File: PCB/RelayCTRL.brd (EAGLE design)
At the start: 46.7 x 22.3 mm, 20 parts, among them Q2 BC848 30V 100mA, Q3 IRLML6402, U1 SN74HC4066D

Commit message: fixed pcb error
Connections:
- removed net N$1: B1.9, R2.2
- net 5V: now also R2.2
- net IR: now also B1.9
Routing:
- net N$1: track 13.3 -> 0.00 mm
- net IR: track 6.76 -> 19.3 mm
- net 5V: track 81.3 -> 92.9 mm
- net S1: track 22.2 -> 19.7 mm
- net BT2: track 39.7 -> 38.1 mm

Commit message: PCB Update
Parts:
- added Q1: BC848 30V 100mA, SparkFun-DiscreteSemi:SOT23-3
- added R7: 1k, rcl:R0603
- renumbered 5V to BZ+, BZ to IR-, G to BZ-
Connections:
- new net BZ-: BZ-.TP, Q1.3
- new net N$1: B1.9, R2.2
- new net N$5: Q1.1, R7.2
- net 5V: no longer R2.2
- net GND: now also IR-.TP, Q1.2, U1.11, U1.8; no longer BZ-.TP
- net IR: no longer B1.9
- net S1: now also R7.1; no longer IR-.TP
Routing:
- net BZ-: track 0.00 -> 37.3 mm, vias 0 -> 1
- net S1: track 19.7 -> 4.01 mm
- net N$1: track 0.00 -> 13.3 mm
- net IR: track 19.3 -> 6.76 mm
- net 5V: track 92.9 -> 81.3 mm
- net N$5: track 0.00 -> 10.3 mm
- net BT2: track 38.1 -> 39.4 mm
- net BT4: track 16.1 -> 17.2 mm
- net SCL: track 24.9 -> 24.7 mm, vias 1 -> 0

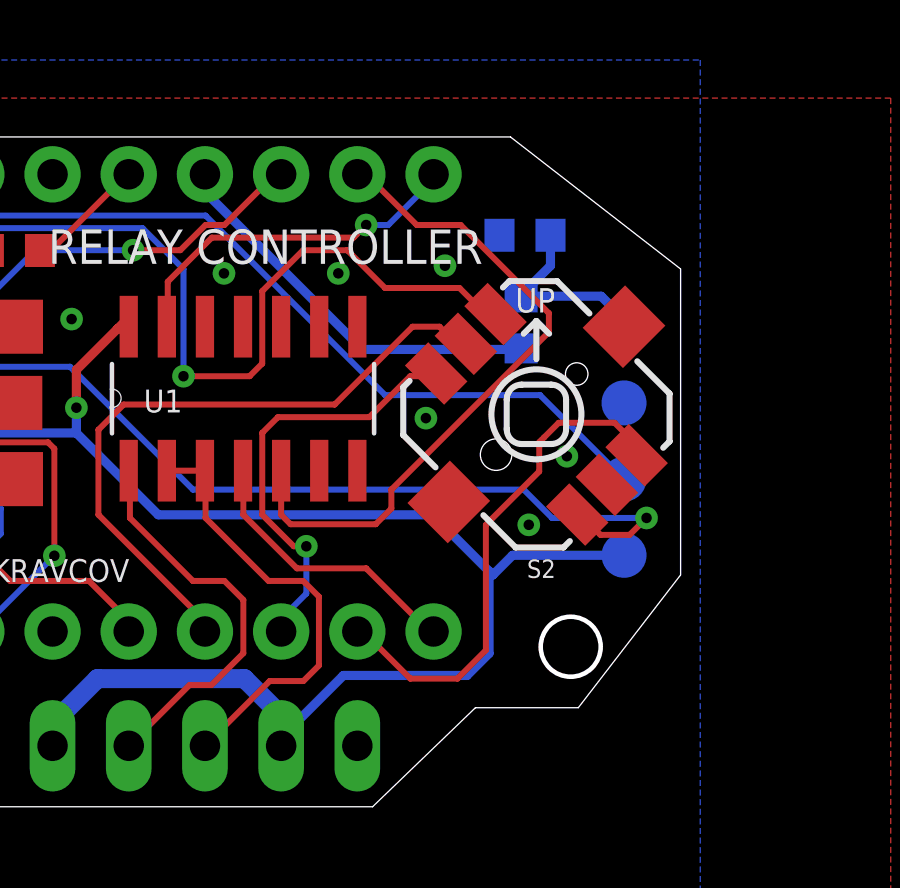
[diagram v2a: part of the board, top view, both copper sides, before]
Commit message: Corrected PCB bug (IR diode)
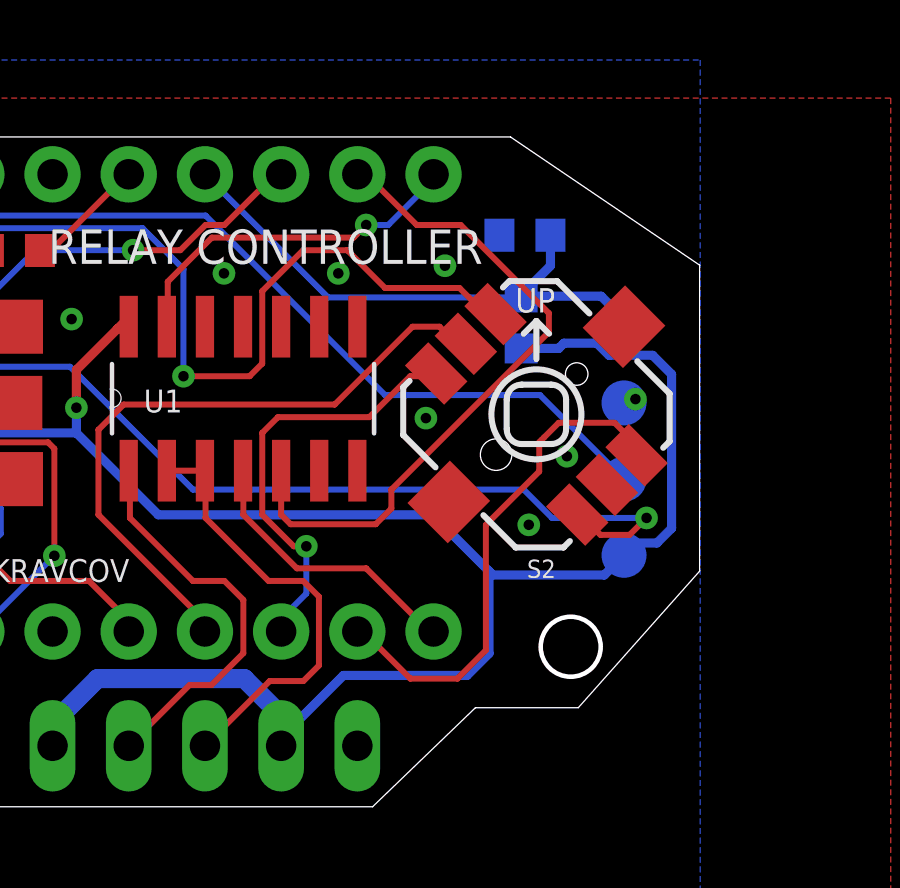
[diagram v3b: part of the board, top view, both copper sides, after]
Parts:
- moved IR+ 2.79 mm to (38.1, 100.3)
- moved IR- 2.79 mm to (38.1, 103.1)
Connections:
- removed net N$1: B1.9, R2.2
- net 5V: now also R2.2
- net GND: now also IR+.TP; no longer IR-.TP
- net IR: now also B1.9, IR-.TP; no longer IR+.TP
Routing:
- net N$1: track 13.3 -> 0.00 mm
- net 5V: track 81.3 -> 93.9 mm
- net IR: track 6.76 -> 19.0 mm
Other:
- board size 46.7 x 22.3 mm -> 47.4 x 22.3 mm
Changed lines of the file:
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@@
 <drawing>
 <settings>
-<setting alwaysvectorfont="no"/>
+<setting alwaysvectorfont="yes"/>
 <setting verticaltext="up"/>
 </settings>
 <grid distance="50" unitdist="mil" unit="mil" style="lines" multiple="1" display="no" altdistance="5" altunitdist="mil" altunit="mil"/>
 <layers>
-<layer number="1" name="Top" color="4" fill="1" visible="yes" active="yes"/>
+<layer number="1" name="Top" color="4" fill="1" visible="no" active="yes"/>
 <layer number="2" name="Route2" color="16" fill="1" visible="no" active="no"/>
 <layer number="3" name="Route3" color="17" fill="1" visible="no" active="no"/>
@@
 <layer number="14" name="Route14" color="22" fill="1" visible="no" active="no"/>
 <layer number="15" name="Route15" color="23" fill="1" visible="no" active="no"/>
-<layer number="16" name="Bottom" color="1" fill="1" visible="no" active="yes"/>
+<layer number="16" name="Bottom" color="1" fill="1" visible="yes" active="yes"/>
 <layer number="17" name="Pads" color="2" fill="1" visible="yes" active="yes"/>
 <layer number="18" name="Vias" color="2" fill="1" visible="yes" active="yes"/>
 <layer number="19" name="Unrouted" color="6" fill="1" visible="yes" active="yes"/>
 <layer number="20" name="Dimension" color="24" fill="1" visible="yes" active="yes"/>
-<layer number="21" name="tPlace" color="7" fill="1" visible="yes" active="yes"/>
-<layer number="22" name="bPlace" color="7" fill="1" visible="no" active="yes"/>
-<layer number="23" name="tOrigins" color="15" fill="1" visible="yes" active="yes"/>
-<layer number="24" name="bOrigins" color="15" fill="1" visible="no" active="yes"/>
-<layer number="25" name="tNames" color="7" fill="1" visible="yes" active="yes"/>
-<layer number="26" name="bNames" color="7" fill="1" visible="no" active="yes"/>
+<layer number="21" name="tPlace" color="7" fill="1" visible="no" active="yes"/>
+<layer number="22" name="bPlace" color="7" fill="1" visible="yes" active="yes"/>
+<layer number="23" name="tOrigins" color="15" fill="1" visible="no" active="yes"/>
+<layer number="24" name="bOrigins" color="15" fill="1" visible="yes" active="yes"/>
+<layer number="25" name="tNames" color="7" fill="1" visible="no" active="yes"/>
+<layer number="26" name="bNames" color="7" fill="1" visible="yes" active="yes"/>
 <layer number="27" name="tValues" color="7" fill="1" visible="no" active="yes"/>
 <layer number="28" name="bValues" color="7" fill="1" visible="no" active="yes"/>
@@
 <layer number="37" name="tTest" color="7" fill="1" visible="no" active="yes"/>
 <layer number="38" name="bTest" color="7" fill="1" visible="no" active="yes"/>
-<layer number="39" name="tKeepout" color="4" fill="11" visible="yes" active="yes"/>
-<layer number="40" name="bKeepout" color="1" fill="11" visible="no" active="yes"/>
-<layer number="41" name="tRestrict" color="4" fill="10" visible="yes" active="yes"/>
-<layer number="42" name="bRestrict" color="1" fill="10" visible="no" active="yes"/>
+<layer number="39" name="tKeepout" color="4" fill="11" visible="no" active="yes"/>
+<layer number="40" name="bKeepout" color="1" fill="11" visible="yes" active="yes"/>
+<layer number="41" name="tRestrict" color="4" fill="10" visible="no" active="yes"/>
+<layer number="42" name="bRestrict" color="1" fill="10" visible="yes" active="yes"/>
 <layer number="43" name="vRestrict" color="2" fill="10" visible="no" active="yes"/>
 <layer number="44" name="Drills" color="7" fill="1" visible="no" active="yes"/>
@@
 <layer number="49" name="Reference" color="7" fill="1" visible="no" active="yes"/>
 <layer number="50" name="dxf" color="7" fill="1" visible="no" active="no"/>
-<layer number="51" name="tDocu" color="7" fill="1" visible="yes" active="yes"/>
-<layer number="52" name="bDocu" color="7" fill="1" visible="no" active="yes"/>
+<layer number="51" name="tDocu" color="7" fill="1" visible="no" active="yes"/>
+<layer number="52" name="bDocu" color="7" fill="1" visible="yes" active="yes"/>
 <layer number="53" name="tGND_GNDA" color="7" fill="9" visible="no" active="no"/>
 <layer number="54" name="bGND_GNDA" color="1" fill="9" visible="no" active="no"/>
@@
 <wire x1="29.718" y1="86.868" x2="33.147" y2="90.17" width="0" layer="20"/>
 <wire x1="33.147" y1="90.17" x2="36.576" y2="90.17" width="0" layer="20"/>
-<wire x1="36.576" y1="90.17" x2="39.985" y2="94.595" width="0" layer="20"/>
-<wire x1="39.985" y1="94.595" x2="39.985" y2="104.795" width="0" layer="20"/>
-<wire x1="39.985" y1="104.795" x2="34.3152" y2="109.1948" width="0" layer="20"/>
+<wire x1="36.576" y1="90.17" x2="40.62" y2="94.722" width="0" layer="20"/>
+<wire x1="40.62" y1="94.722" x2="40.62" y2="104.922" width="0" layer="20"/>
+<wire x1="40.62" y1="104.922" x2="34.3152" y2="109.1948" width="0" layer="20"/>
 <wire x1="34.3152" y1="109.1948" x2="-1.2952" y2="109.1948" width="0" layer="20"/>
 <wire x1="-1.2952" y1="109.1948" x2="-6.731" y2="103.759" width="0" layer="20"/>
@@
 <attribute name="VALUE" x="15.24" y="97.79" size="1.27" layer="27"/>
 </element>
-<element name="IR+" library="testpad" library_urn="urn:adsk.eagle:library:385" package="TP15R" package3d_urn="urn:adsk.eagle:package:27968/1" value="TPTP15R" x="38.1" y="103.124" smashed="yes" rot="MR0">
+<element name="IR-" library="testpad" library_urn="urn:adsk.eagle:library:385" package="TP15R" package3d_urn="urn:adsk.eagle:package:27968/1" value="TPTP15R" x="38.1" y="103.124" smashed="yes" rot="MR0">
 <attribute name="NAME" x="36.9451" y="102.9081" size="0.762" layer="26" ratio="10" rot="MR0"/>
 <attribute name="POPULARITY" value="0" x="38.1" y="103.124" size="1.778" layer="28" rot="MR0" display="off"/>
@@
 <attribute name="VALUE" x="38.735" y="94.488" size="0.0254" layer="28" rot="MR0"/>
 </element>
-<element name="IR-" library="testpad" library_urn="urn:adsk.eagle:library:385" package="TP15R" package3d_urn="urn:adsk.eagle:package:27968/1" value="TPTP15R" x="38.1" y="100.33" smashed="yes" rot="MR0">
+<element name="IR+" library="testpad" library_urn="urn:adsk.eagle:library:385" package="TP15R" package3d_urn="urn:adsk.eagle:package:27968/1" value="TPTP15R" x="38.1" y="100.33" smashed="yes" rot="MR0">
 <attribute name="NAME" x="36.9451" y="99.8601" size="0.762" layer="26" ratio="10" rot="MR0"/>
 <attribute name="POPULARITY" value="0" x="38.1" y="100.33" size="1.778" layer="28" rot="MR0" display="off"/>
@@
 <via x="-3.175" y="105.156" extent="1-16" drill="0.35"/>
 <via x="-0.635" y="101.346" extent="1-16" drill="0.35"/>
-<contactref element="IR-" pad="TP"/>
+<contactref element="IR+" pad="TP"/>
 <via x="34.925" y="96.266" extent="1-16" drill="0.35"/>
 <contactref element="R6" pad="1"/>
@@
 <contactref element="U1" pad="11"/>
 <via x="24.765" y="104.648" extent="1-16" drill="0.35"/>
+<via x="38.481" y="100.457" extent="1-16" drill="0.35"/>
 </signal>
 <signal name="5V" class="2">
@@
 <wire x1="31.72" y1="96.6" x2="33.6" y2="94.72" width="0.3048" layer="16"/>
 <wire x1="33.6" y1="94.72" x2="33.727" y2="94.593" width="0.3048" layer="16"/>
-<wire x1="38.1" y1="95.25" x2="34.384" y2="95.25" width="0.3048" layer="16"/>
-<wire x1="34.384" y1="95.25" x2="33.727" y2="94.593" width="0.3048" layer="16"/>
+<wire x1="38.1" y1="95.25" x2="37.443" y2="94.593" width="0.3048" layer="16"/>
+<wire x1="37.443" y1="94.593" x2="33.727" y2="94.593" width="0.3048" layer="16"/>
 <wire x1="22.575" y1="96.6" x2="31.72" y2="96.6" width="0.3048" layer="16"/>
 <via x="19.845" y="100.17" extent="1-16" drill="0.35"/>
@@
 <wire x1="3.78" y1="92.715" x2="3.81" y2="92.71" width="0.3048" layer="1"/>
 <contactref element="BZ+" pad="TP"/>
+<contactref element="R2" pad="2"/>
+<wire x1="34.671" y1="102.147" x2="35.92403125" y2="102.147" width="0.3048" layer="16"/>
+<wire x1="35.92403125" y1="102.147" x2="36.09693125" y2="102.3199" width="0.3048" layer="16"/>
+<wire x1="37.5999625" y1="101.9168" x2="39.0532" y2="101.9168" width="0.3048" layer="16"/>
+<wire x1="36.09693125" y1="102.3199" x2="37.1968625" y2="102.3199" width="0.3048" layer="16"/>
+<wire x1="37.1968625" y1="102.3199" x2="37.5999625" y2="101.9168" width="0.3048" layer="16"/>
+<wire x1="39.6854" y1="96.1489625" x2="39.1960375" y2="95.6596" width="0.3048" layer="16"/>
+<wire x1="39.1960375" y1="95.6596" x2="38.5096" y2="95.6596" width="0.3048" layer="16"/>
+<wire x1="38.5096" y1="95.6596" x2="38.1" y2="95.25" width="0.3048" layer="16"/>
+<wire x1="39.0532" y1="101.9168" x2="39.6854" y2="101.2846" width="0.3048" layer="16"/>
+<wire x1="39.6854" y1="101.2846" x2="39.6854" y2="96.1489625" width="0.3048" layer="16"/>
 </signal>
 <signal name="SDA">
@@
 <wire x1="21.525" y1="107.94" x2="21.59" y2="107.95" width="0.2" layer="1"/>
 </signal>
-<signal name="N$1">
-<contactref element="B1" pad="9"/>
-<contactref element="R2" pad="2"/>
-<wire x1="34.671" y1="102.147" x2="34.63559375" y2="102.11159375" width="0.3048" layer="16"/>
-<wire x1="34.63559375" y1="102.11159375" x2="29.382675" y2="102.11159375" width="0.3048" layer="16"/>
-<wire x1="29.382675" y1="102.11159375" x2="24.13" y2="107.36426875" width="0.3048" layer="16"/>
-<wire x1="24.13" y1="107.95" x2="24.13" y2="107.36426875" width="0.3048" layer="16"/>
-</signal>
 <signal name="3V">
 <contactref element="B1" pad="21"/>
@@
 <contactref element="R2" pad="1"/>
 <contactref element="R6" pad="2"/>
-<contactref element="IR+" pad="TP"/>
+<contactref element="IR-" pad="TP"/>
 <wire x1="38.1" y1="102.489" x2="38.1" y2="103.124" width="0.2" layer="16"/>
 <wire x1="38.1" y1="103.124" x2="37.338" y2="103.886" width="0.3048" layer="16"/>
@@
 <wire x1="35.648" y1="105.918" x2="35.648" y2="104.902" width="0.3048" layer="16"/>
 <wire x1="34.671" y1="103.847" x2="34.71" y2="103.886" width="0.2" layer="16"/>
+<contactref element="B1" pad="9"/>
+<wire x1="34.671" y1="103.847" x2="28.233" y2="103.847" width="0.2" layer="16"/>
+<wire x1="28.233" y1="103.847" x2="24.13" y2="107.95" width="0.2" layer="16"/>
 </signal>
 <signal name="N$5">
